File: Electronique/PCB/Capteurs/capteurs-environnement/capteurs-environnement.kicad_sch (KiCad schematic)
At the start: 4 parts, among them U1 Pico, U2 STEMMA, U3 STEMMA, U4 STEMMA

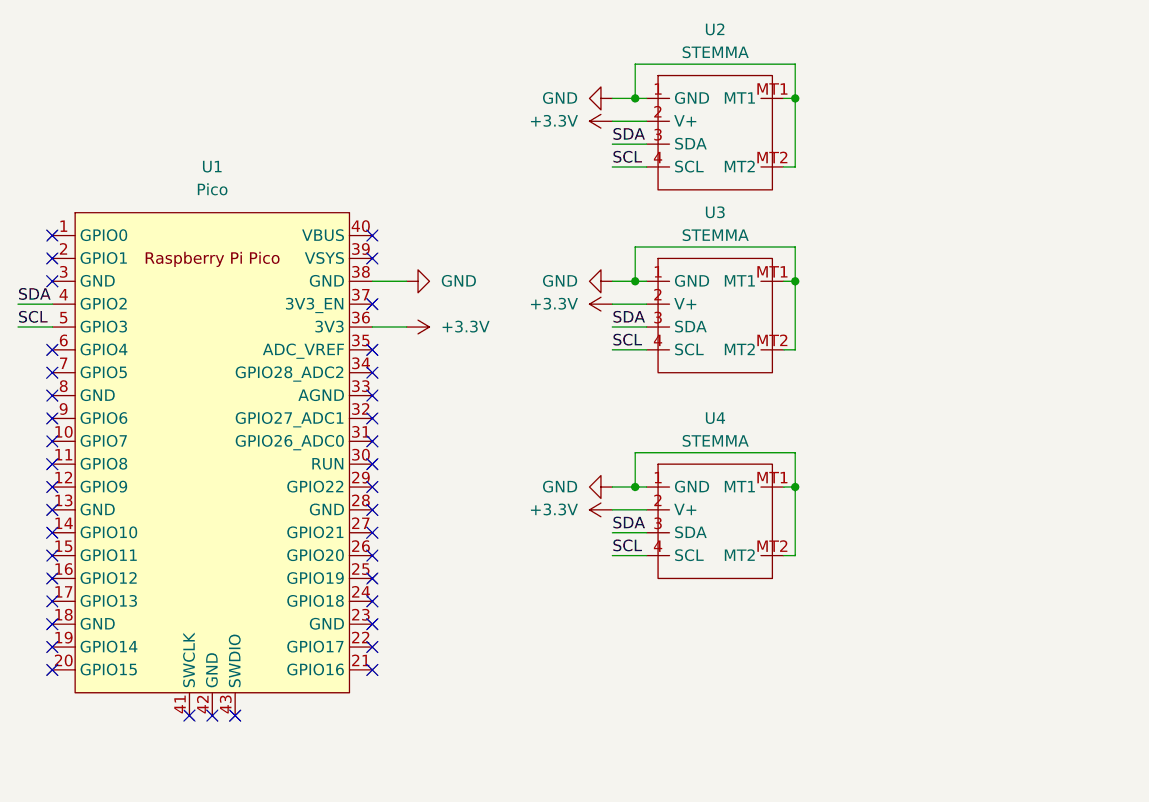
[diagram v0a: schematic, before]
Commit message: update to pcb for environnement sensors + external libs
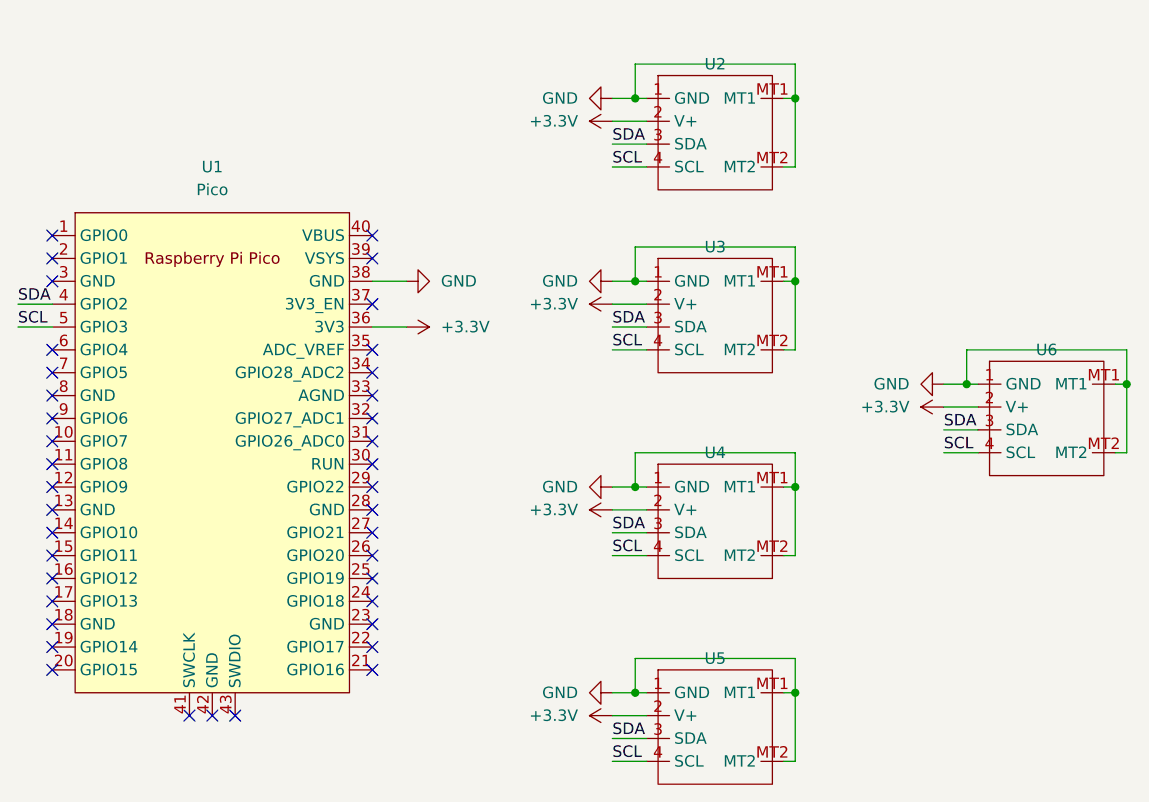
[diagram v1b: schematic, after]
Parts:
- removed U2, U3, U4: STEMMA, Adafruit MS8607:JST_SH4, symbol capteurs-environnement:STEMMA
- added U2, U3, U4, U5, U6: ~, Connectors:JST_SH4, symbol Connectors:JST_SH4
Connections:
- net +3.3V: now also U2.2 (V+), U3.2 (V+), U4.2 (V+), U5.2 (V+), U6.2 (V+)
- net GND: now also U2.1 (GND), U2.MT1, U2.MT2, U3.1 (GND), U3.MT1, U3.MT2, U4.1 (GND), U4.MT1, U4.MT2, U5.1 (GND), U5.MT1, U5.MT2, U6.1 (GND), U6.MT1, U6.MT2
- net SCL: now also U2.4 (SCL), U3.4 (SCL), U4.4 (SCL), U5.4 (SCL), U6.4 (SCL)
- net SDA: now also U2.3 (SDA), U3.3 (SDA), U4.3 (SDA), U5.3 (SDA), U6.3 (SDA)

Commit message: pcb updates
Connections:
- net GND: no longer U2.MT1, U2.MT2, U3.MT1, U3.MT2, U4.MT1, U4.MT2, U5.MT1, U5.MT2, U6.MT1, U6.MT2
- no-connect marks 39 -> 49
